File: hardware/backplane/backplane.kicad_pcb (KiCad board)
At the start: 2 copper layers, 100 x 50 mm, 50 parts, among them J1 Conn_01x04_Male, J10 Conn_02x10_Odd_Even, J13 Conn_01x08_Male, J2 RJ45_LED, J5 RJ45_LED, J6 Raspberry_Pi_2_3, J9 Conn_02x10_Odd_Even, U1 TXB0102DCU, U2 TXB0102DCU, U3 TXB0102DCU, U4 MCP23017_SO, U5 WAVGAT_CAN

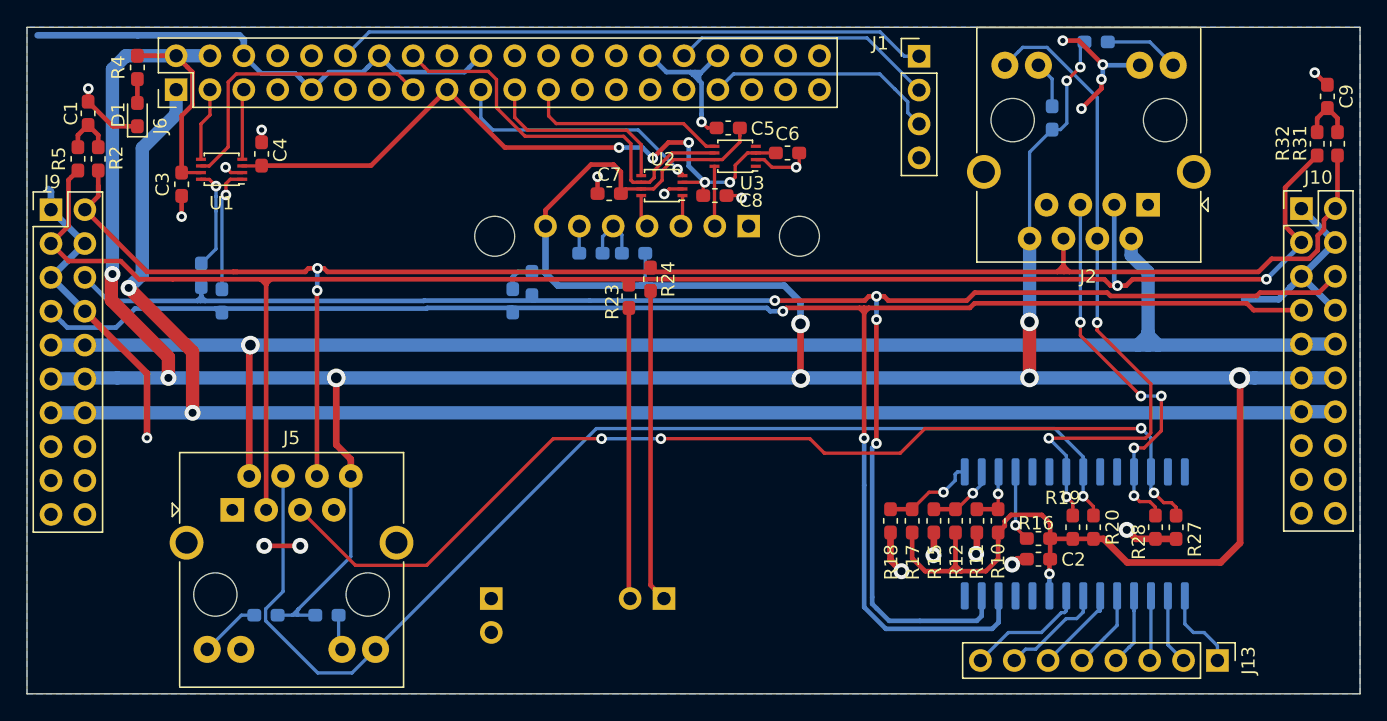
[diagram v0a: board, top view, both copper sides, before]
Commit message: Reorient RJ45 connectors in backplane, make interrupt pins accessible in IO Expanders
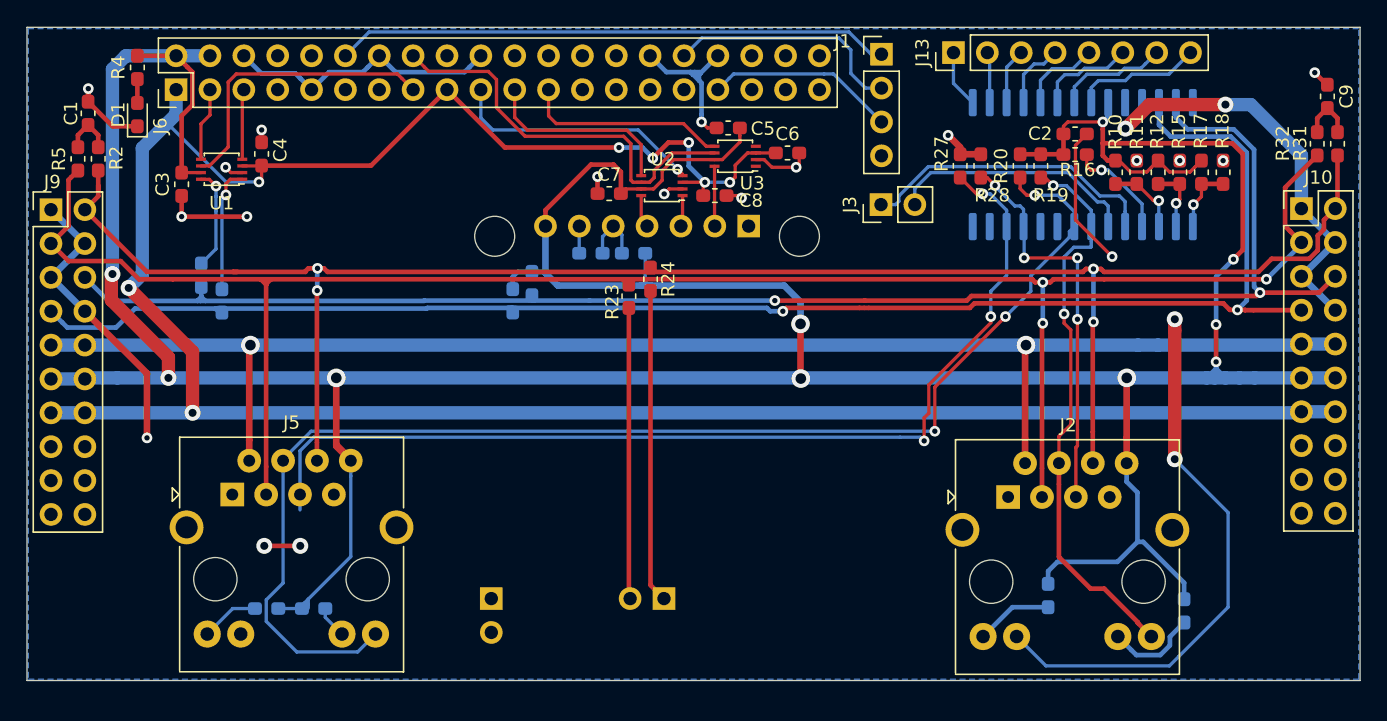
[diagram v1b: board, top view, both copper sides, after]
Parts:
- added J3: Conn_01x02_Male-Connector, Connector_PinHeader_2.54mm:PinHeader_1x02_P2.54mm_Vertical, F.Cu at (144.1, 83.3)
- moved J13 49.7 mm to (149.5, 71.9), turned to 90 degrees
- moved R3 41.7 mm to (156.6, 112.6), turned to 270 degrees
- moved R1 38.3 mm to (166.8, 113.8), turned to 270 degrees
- moved R18 36.1 mm to (169.7, 80.9), turned to 90 degrees
- moved R17 34.0 mm to (168.1, 80.9), turned to 90 degrees
- moved C2 32.0 mm to (158.6, 78.0), turned to 0 degrees
- moved R15 32.0 mm to (166.5, 80.9), turned to 90 degrees
- moved R27 31.6 mm to (150.0, 80.4), turned to 270 degrees
- moved R12 30.2 mm to (164.8, 80.9), turned to 90 degrees
- moved R28 30.1 mm to (151.6, 80.4), turned to 270 degrees
- moved R16 28.9 mm to (158.6, 79.5), turned to 180 degrees
- moved R11 28.8 mm to (163.2, 80.9), turned to 90 degrees
- moved U4 27.7 mm to (159.2, 80.3), turned to 270 degrees
- moved R20 27.7 mm to (154.5, 80.4), turned to 90 degrees
- moved R10 27.6 mm to (161.7, 80.9), turned to 90 degrees
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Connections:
- U4 pad 19: (no net) -> Net-(J3-Pad1)
- U4 pad 20: (no net) -> Net-(J3-Pad2)
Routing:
- net GND: track 137.1 -> 172.1 mm, vias 22 -> 23
- net Net-(J3-Pad1): track 0.00 -> 22.7 mm
- net Net-(J3-Pad2): track 0.00 -> 18.8 mm
- net /SCL: track 135.2 -> 118.0 mm
- net /SDA: track 131.8 -> 116.6 mm, vias 4 -> 2
- net WIRE_GOOD_1: track 87.6 -> 98.6 mm, vias 1 -> 3
- net +3V3: track 175.5 -> 185.6 mm, vias 7 -> 8
- net /CANBUS_HIGH: track 128.2 -> 138.0 mm, vias 2 -> 4
- net /CANBUS_LOW: track 135.7 -> 144.3 mm, vias 2 -> 3
- net WIRE_GOOD_0: track 50.2 -> 42.4 mm, vias 3 -> 2
- net Net-(J2-Pad10): track 3.50 -> 6.94 mm
- net Net-(J1-Pad3): track 17.6 -> 14.3 mm
- net +12V: track 117.0 -> 113.9 mm, vias 1 -> 2
- net Net-(J1-Pad1): track 44.5 -> 41.6 mm
- net Net-(R16-Pad1): track 5.35 -> 7.88 mm
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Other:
- board size 100 x 50 mm -> 100 x 49 mm

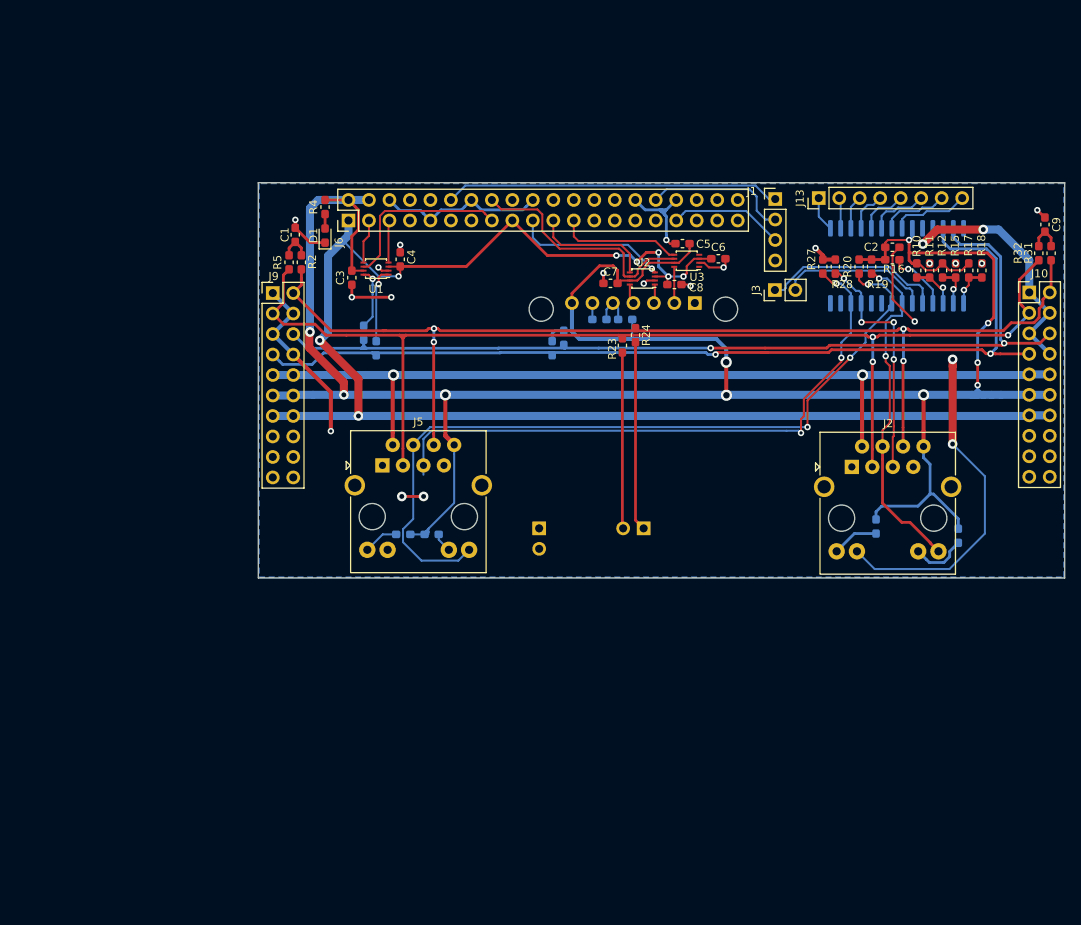
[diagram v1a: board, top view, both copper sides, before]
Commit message: New backplane schematic
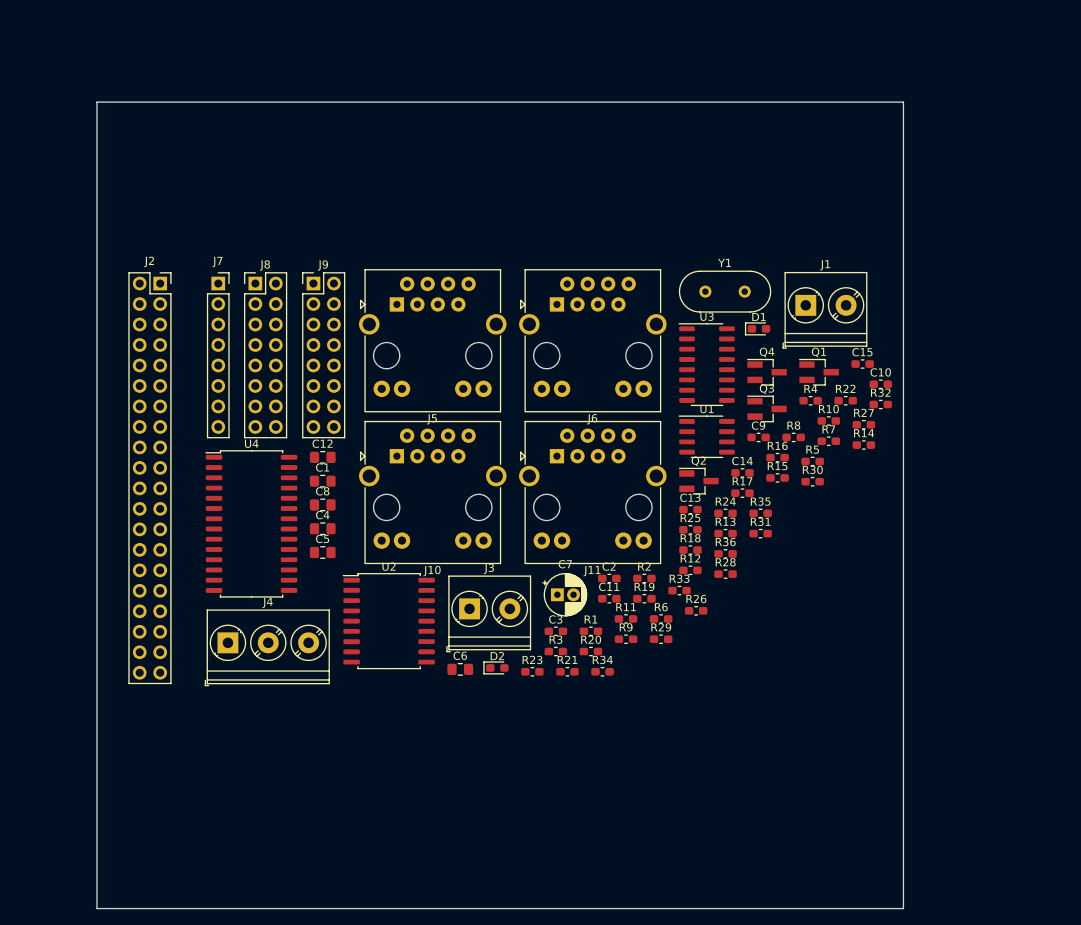
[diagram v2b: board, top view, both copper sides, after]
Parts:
- removed J13: Conn_01x08_Male, Connector_PinHeader_2.54mm:PinHeader_1x08_P2.54mm_Vertical
- removed U5: WAVGAT_CAN, WAVGAT_CAN:WAVGAT_CAN
- added C10: 100n, Capacitor_SMD:C_0603_1608Metric_Pad1.05x0.95mm_HandSolder, F.Cu at (157.2, 95.0)
- added C11: 22p, Capacitor_SMD:C_0603_1608Metric_Pad1.05x0.95mm_HandSolder, F.Cu at (123.5, 121.6)
- added C12: 470n, Capacitor_SMD:C_0805_2012Metric_Pad1.15x1.40mm_HandSolder, F.Cu at (88.0, 104.0)
- added C13: 4n7, Capacitor_SMD:C_0603_1608Metric_Pad1.05x0.95mm_HandSolder, F.Cu at (133.6, 110.5)
- added C14: 4n7, Capacitor_SMD:C_0603_1608Metric_Pad1.05x0.95mm_HandSolder, F.Cu at (140.0, 106.0)
- added C15: 100n, Capacitor_SMD:C_0603_1608Metric_Pad1.05x0.95mm_HandSolder, F.Cu at (154.9, 92.5)
- added D2: LED, LED_SMD:LED_0603_1608Metric_Pad1.05x0.95mm_HandSolder, F.Cu at (109.6, 130.2)
- added J11: RJ45_LED, Connector_RJ:RJ45_BEL_SS74301-00x_Vertical, F.Cu at (117.0, 103.9)
- added J4: Screw_Terminal_01x03, TerminalBlock_Phoenix:TerminalBlock_Phoenix_PT-1,5-3-5.0-H_1x03_P5.00mm_Horizontal, F.Cu at (76.2, 127.0)
- added J7: Conn_01x08_Female, Connector_PinSocket_2.54mm:PinSocket_1x08_P2.54mm_Vertical, F.Cu at (75.0, 82.5)
- added J8: Conn_02x08_Odd_Even, Connector_PinHeader_2.54mm:PinHeader_2x08_P2.54mm_Vertical, F.Cu at (79.6, 82.5)
- added Q1: Q_NMOS_GSD, Package_TO_SOT_SMD:SOT-23_Handsoldering, F.Cu at (149.5, 93.5)
- added Q2: Q_NMOS_GSD, Package_TO_SOT_SMD:SOT-23_Handsoldering, F.Cu at (134.6, 107.0)
- added Q3: Q_NMOS_GSD, Package_TO_SOT_SMD:SOT-23_Handsoldering, F.Cu at (143.1, 98.0)
- added Q4: Q_NMOS_GSD, Package_TO_SOT_SMD:SOT-23_Handsoldering, F.Cu at (143.1, 93.5)
- added R21: 560R, Resistor_SMD:R_0603_1608Metric_Pad1.05x0.95mm_HandSolder, F.Cu at (118.3, 130.6)
- added R22: 60R, Resistor_SMD:R_0603_1608Metric_Pad1.05x0.95mm_HandSolder, F.Cu at (152.8, 97.0)
- added R25: 560R, Resistor_SMD:R_0603_1608Metric_Pad1.05x0.95mm_HandSolder, F.Cu at (133.6, 113.0)
- added R26: 4K7, Resistor_SMD:R_0603_1608Metric_Pad1.05x0.95mm_HandSolder, F.Cu at (134.3, 123.1)
- added R33: 4K7, Resistor_SMD:R_0603_1608Metric_Pad1.05x0.95mm_HandSolder, F.Cu at (132.2, 120.6)
- added R34: 4K7, Resistor_SMD:R_0603_1608Metric_Pad1.05x0.95mm_HandSolder, F.Cu at (122.7, 130.6)
- added R35: 4K7, Resistor_SMD:R_0603_1608Metric_Pad1.05x0.95mm_HandSolder, F.Cu at (142.3, 111.0)
- added R36: 4K7, Resistor_SMD:R_0603_1608Metric_Pad1.05x0.95mm_HandSolder, F.Cu at (137.9, 116.0)
- added Y1: 8MHz, Crystal:Crystal_HC49-U_Vertical, F.Cu at (135.4, 83.5)
- C1: value 4n7 -> 10u; footprint Capacitor_SMD:C_0603_1608Metric_Pad1.05x0.95mm_HandSolder -> Capacitor_SMD:C_0805_2012Metric_Pad1.15x1.40mm_HandSolder
- C2, C3: value 0.1uF -> 100n
- C4, C5, C6: value 0.1uF -> 1u; footprint Capacitor_SMD:C_0603_1608Metric_Pad1.05x0.95mm_HandSolder -> Capacitor_SMD:C_0805_2012Metric_Pad1.15x1.40mm_HandSolder
- C7: value 0.1uF -> 47u; footprint Capacitor_SMD:C_0603_1608Metric_Pad1.05x0.95mm_HandSolder -> Capacitor_THT:CP_Radial_D5.0mm_P2.00mm
- C8: value 0.1uF -> 470n; footprint Capacitor_SMD:C_0603_1608Metric_Pad1.05x0.95mm_HandSolder -> Capacitor_SMD:C_0805_2012Metric_Pad1.15x1.40mm_HandSolder
- C9: value 4n7 -> 22p
- J1: value Conn_01x04_Male -> Screw_Terminal_01x02; footprint Connector_PinHeader_2.54mm:PinHeader_1x04_P2.54mm_Vertical -> TerminalBlock_Phoenix:TerminalBlock_Phoenix_PT-1,5-2-5.0-H_1x02_P5.00mm_Horizontal
- J10: value Conn_02x10_Odd_Even -> RJ45_LED; footprint Connector_PinHeader_2.54mm:PinHeader_2x10_P2.54mm_Vertical -> Connector_RJ:RJ45_BEL_SS74301-00x_Vertical
- J2: value RJ45_LED -> Raspberry_Pi_2_3; footprint Connector_RJ:RJ45_BEL_SS74301-00x_Vertical -> Connector_PinSocket_2.54mm:PinSocket_2x20_P2.54mm_Vertical
- J3: value Conn_01x02_Male-Connector -> Screw_Terminal_01x02; footprint Connector_PinHeader_2.54mm:PinHeader_1x02_P2.54mm_Vertical -> TerminalBlock_Phoenix:TerminalBlock_Phoenix_PT-1,5-2-5.0-H_1x02_P5.00mm_Horizontal
- J6: value Raspberry_Pi_2_3 -> RJ45_LED; footprint Connector_PinHeader_2.54mm:PinHeader_2x20_P2.54mm_Vertical -> Connector_RJ:RJ45_BEL_SS74301-00x_Vertical
- J9: value Conn_02x10_Odd_Even -> Conn_02x08_Odd_Even; footprint Connector_PinHeader_2.54mm:PinHeader_2x10_P2.54mm_Vertical -> Connector_PinHeader_2.54mm:PinHeader_2x08_P2.54mm_Vertical
- R1, R8, R9: value 560R -> 10k; moved to F.Cu
- R10: value 4K7 -> 560R
- R11: value 4K7 -> 2k
- R12, R15: value 4K7 -> 10k
- R13, R14: value 0R -> 10k; moved to F.Cu
- R16, R17: value 4K7 -> 0R
- R18: value 4K7 -> 60R
- R19: value 10K -> 60R
- R2, R5: value 60R -> 10k
- R20, R27, R28: value 10K -> 560R
- R23: value 0R -> 60R
- R24: value 0R -> 560R
- R29, R30: value 4K7 -> 560R; moved to F.Cu
- R3: value 560R -> 0R; moved to F.Cu
- R31, R32: value 60R -> 4K7
- R4: value 560R -> 0R
- R6, R7: value 4K7 -> 10k; moved to F.Cu
- U1: value TXB0102DCU -> TJA1051T; footprint Package_SO:VSSOP-8_2.4x2.1mm_P0.5mm -> Package_SO:SOIC-8_3.9x4.9mm_P1.27mm
- U2: value TXB0102DCU -> MCP2515-xSO; footprint Package_SO:VSSOP-8_2.4x2.1mm_P0.5mm -> Package_SO:SOIC-18W_7.5x11.6mm_P1.27mm
- U3: value TXB0102DCU -> PAM8403; footprint Package_SO:VSSOP-8_2.4x2.1mm_P0.5mm -> Package_SO:SOIC-16_3.9x9.9mm_P1.27mm
- U4: moved to F.Cu
- moved J2 88.7 mm to (67.8, 82.5)
- moved U4 86.2 mm to (79.2, 112.3), turned to 0 degrees
- moved J10 81.0 mm to (97.2, 103.9)
- moved R5 69.5 mm to (148.7, 104.6), turned to 0 degrees
- moved R4 64.8 mm to (148.5, 97.0), turned to 0 degrees
- moved R14 63.6 mm to (155.1, 102.5), turned to 0 degrees
- moved C6 60.1 mm to (105.0, 130.3)
- moved C5 58.8 mm to (88.0, 115.8)
- moved R20 58.2 mm to (121.2, 128.1), turned to 0 degrees
- moved R2 57.8 mm to (127.9, 119.1), turned to 0 degrees
- moved R11 57.3 mm to (125.6, 124.1), turned to 0 degrees
- moved D1 55.0 mm to (142.1, 88.1), turned to 0 degrees
- moved J3 54.7 mm to (106.2, 122.8), turned to 0 degrees
- moved C2 54.0 mm to (123.5, 119.1)
- moved U2 52.8 mm to (96.2, 124.4), turned to 0 degrees
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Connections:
- C1 pad 1: GND -> +3V3
- C1 pad 2: Net-(C1-Pad2) -> GND
- C3 pad 1: GND -> +3V3
- C3 pad 2: VCC -> GND
- C4 pad 1: +3V3 -> VCC
- C5 pad 1: GND -> VCC
- C5 pad 2: VCC -> GND
- C6 pad 1: +3V3 -> VCC
- C7 pad 1: GND -> VCC
- C7 pad 2: VCC -> GND
- C8 pad 1: +3V3 -> Net-(C8-Pad1)
- C8 pad 2: GND -> AUDIO_L
- C9 pad 1: GND -> Net-(C9-Pad1)
- C9 pad 2: Net-(C9-Pad2) -> GND
- J1 pad 1: Net-(J1-Pad1) -> /SPKR_L+
- J1 pad 2: Net-(J1-Pad2) -> /SPKR_L-
- J10 pad 10: +12V -> Net-(J10-Pad10)
- J10 pad 11: VCC -> MODULE_READY_2
- J10 pad 12: VCC -> Net-(J10-Pad12)
- J10 pad 2: /CANBUS_HIGH -> +12V
- J10 pad 3: /CANBUS_LOW -> CAN_L
- J10 pad 4: GND -> MODULE_READY_2
- J10 pad 5: GND -> MODULE_ENABLE_2
- J10 pad 6: /SDA -> CAN_H
- J10 pad 7: /SCL -> GND
- J10 pad 8: GND -> VCC
- J10 pad 9: +12V -> MODULE_ENABLE_2
- J2 pad 1: GND -> +3V3
- J2 pad 11: GND -> Net-(J2-Pad11)
- J2 pad 2: +12V -> VCC
- J2 pad 3: /CANBUS_LOW -> SDA_3V3
- J2 pad 4: WIRE_GOOD_0 -> VCC
- J2 pad 5: MODULE_GOOD_0 -> SCL_3V3
- J2 pad 6: /CANBUS_HIGH -> GND
- J2 pad 7: GND -> Net-(J2-Pad7)
- J2 pad 8: VCC -> Net-(J2-Pad8)
- J2 pad 9: WIRE_GOOD_0 -> GND
- J3 pad 1: Net-(J3-Pad1) -> /SPKR_R-
- J3 pad 2: Net-(J3-Pad2) -> /SPKR_R+
- J5 pad 11: GND -> MODULE_READY_0
- J5 pad 3: /CANBUS_LOW -> CAN_L
- J5 pad 4: WIRE_GOOD_1 -> MODULE_READY_0
- J5 pad 5: MODULE_GOOD_1 -> MODULE_ENABLE_0
- J5 pad 6: /CANBUS_HIGH -> CAN_H
- J5 pad 9: WIRE_GOOD_1 -> MODULE_ENABLE_0
- J5 pad SH: (no net) -> GND
- J6 pad 1: +3V3 -> GND
- J6 pad 10: (no net) -> Net-(J6-Pad10)
- J6 pad 11: (no net) -> MODULE_READY_1
- J6 pad 12: Net-(J1-Pad1) -> Net-(J6-Pad12)
- J6 pad 2: VCC -> +12V
- J6 pad 3: Net-(J6-Pad3) -> CAN_L
- J6 pad 4: VCC -> MODULE_READY_1
- J6 pad 5: Net-(J6-Pad5) -> MODULE_ENABLE_1
- J6 pad 6: GND -> CAN_H
- J6 pad 7: (no net) -> GND
- J6 pad 8: (no net) -> VCC
- J6 pad 9: GND -> MODULE_ENABLE_1
- J9 pad 15: (no net) -> Net-(J9-Pad15)
- J9 pad 16: (no net) -> Net-(J9-Pad16)
- J9 pad 2: /CANBUS_HIGH -> CAN_H
- J9 pad 3: /CANBUS_LOW -> CAN_L
- J9 pad 6: /SDA -> SDA
- J9 pad 7: /SCL -> SCL
- R1 pad 1: VCC -> +3V3
- R1 pad 2: Net-(J2-Pad10) -> Net-(Q1-Pad2)
- R10 pad 1: Net-(R10-Pad1) -> VCC
- R10 pad 2: VCC -> Net-(D1-Pad2)
- R11 pad 1: Net-(R10-Pad1) -> +12V
- R11 pad 2: GND -> Net-(D2-Pad2)
- R12 pad 1: Net-(R12-Pad1) -> +3V3
- R12 pad 2: VCC -> SCL_3V3
- R13 pad 1: /SCL -> VCC
- R13 pad 2: Net-(R13-Pad2) -> Net-(Q3-Pad3)
- R14 pad 1: Net-(R14-Pad1) -> +3V3
- R14 pad 2: /SDA -> SDA_3V3
- R15 pad 1: Net-(R12-Pad1) -> VCC
- R15 pad 2: GND -> Net-(Q4-Pad3)
- R16 pad 1: Net-(R16-Pad1) -> SCL
- R16 pad 2: VCC -> Net-(Q3-Pad3)
- R17 pad 1: Net-(R17-Pad1) -> SDA
- R17 pad 2: VCC -> Net-(Q4-Pad3)
- R18 pad 1: Net-(R17-Pad1) -> CAN_H
- R18 pad 2: GND -> Net-(C13-Pad1)
- R19 pad 1: WIRE_GOOD_0 -> CAN_H
- R19 pad 2: VCC -> Net-(C14-Pad1)
- R2 pad 1: /CANBUS_HIGH -> VCC
- R2 pad 2: Net-(C1-Pad2) -> Net-(Q1-Pad3)
- R20 pad 1: WIRE_GOOD_1 -> VCC
- R20 pad 2: VCC -> Net-(J5-Pad10)
- R23 pad 1: /CANBUS_LOW -> CAN_L
- R23 pad 2: Net-(R23-Pad2) -> Net-(C14-Pad1)
- R24 pad 1: Net-(R24-Pad1) -> VCC
- R24 pad 2: /CANBUS_HIGH -> Net-(J5-Pad12)
- R27 pad 1: GND -> VCC
- R27 pad 2: MODULE_GOOD_1 -> Net-(J10-Pad10)
- R28 pad 1: GND -> VCC
- R28 pad 2: MODULE_GOOD_0 -> Net-(J11-Pad10)
- R29 pad 1: Net-(R29-Pad1) -> VCC
- R29 pad 2: GND -> Net-(J10-Pad12)
- R3 pad 1: VCC -> CAN_H
- R3 pad 2: Net-(J2-Pad12) -> Net-(R3-Pad2)
- R30 pad 1: Net-(R29-Pad1) -> VCC
- R30 pad 2: VCC -> Net-(J11-Pad12)
- R31 pad 1: /CANBUS_HIGH -> Net-(R31-Pad1)
- R31 pad 2: Net-(C9-Pad2) -> VCC
- R32 pad 1: /CANBUS_LOW -> Net-(R31-Pad1)
- R32 pad 2: Net-(C9-Pad2) -> GND
- R4 pad 1: Net-(D1-Pad2) -> CAN_L
- R4 pad 2: VCC -> Net-(R4-Pad2)
- R5 pad 1: /CANBUS_LOW -> Net-(R5-Pad1)
- R5 pad 2: Net-(C1-Pad2) -> Net-(C8-Pad1)
- R6 pad 1: /SDA -> +3V3
- R6 pad 2: VCC -> Net-(Q2-Pad2)
- R7 pad 1: /SCL -> VCC
- R7 pad 2: VCC -> Net-(Q2-Pad3)
- R8 pad 1: VCC -> Net-(R8-Pad1)
- R8 pad 2: Net-(J5-Pad10) -> Net-(C12-Pad1)
- R9 pad 1: VCC -> +3V3
- R9 pad 2: Net-(J5-Pad12) -> Net-(R9-Pad2)
- U1 pad 1: Net-(R13-Pad2) -> Net-(Q2-Pad3)
- U1 pad 3: +3V3 -> VCC
- U1 pad 4: Net-(J6-Pad5) -> Net-(Q1-Pad3)
- U1 pad 5: Net-(J6-Pad3) -> Net-(U1-Pad5)
- U1 pad 6: Net-(J6-Pad15) -> Net-(R4-Pad2)
- U1 pad 7: VCC -> Net-(R3-Pad2)
- U1 pad 8: Net-(R14-Pad1) -> Net-(U1-Pad8)
- U2 pad 1: Net-(U2-Pad1) -> Net-(Q2-Pad2)
- U2 pad 2: GND -> Net-(Q1-Pad2)
- U2 pad 3: +3V3 -> Net-(U2-Pad3)
- U2 pad 4: Net-(J6-Pad19) -> Net-(U2-Pad4)
- U2 pad 5: Net-(J6-Pad21) -> Net-(U2-Pad5)
- U2 pad 6: Net-(J6-Pad16) -> Net-(U2-Pad6)
- U2 pad 7: VCC -> Net-(C9-Pad1)
- U3 pad 1: (no net) -> /SPKR_L+
- U3 pad 3: +3V3 -> /SPKR_L-
- U3 pad 4: (no net) -> VCC
- U3 pad 5: Net-(J6-Pad23) -> Net-(U3-Pad5)
- U3 pad 6: Net-(J6-Pad16) -> VCC
- U3 pad 7: VCC -> Net-(R5-Pad1)
- U4 pad 11: (no net) -> Net-(U4-Pad11)
- U4 pad 12: /SCL -> SCL
- U4 pad 13: /SDA -> SDA
- U4 pad 14: (no net) -> Net-(U4-Pad14)
- U4 pad 15: Net-(R17-Pad1) -> Net-(R35-Pad1)
- U4 pad 16: Net-(R12-Pad1) -> Net-(R33-Pad1)
- U4 pad 17: Net-(R10-Pad1) -> Net-(R31-Pad1)
- U4 pad 18: Net-(R16-Pad1) -> Net-(R26-Pad1)
- U4 pad 19: Net-(J3-Pad1) -> Net-(U4-Pad19)
- U4 pad 20: Net-(J3-Pad2) -> MCP23017_INT
- U4 pad 21: WIRE_GOOD_0 -> MODULE_ENABLE_0
- U4 pad 22: WIRE_GOOD_1 -> MODULE_ENABLE_1
- U4 pad 23: (no net) -> MODULE_ENABLE_2
- U4 pad 24: (no net) -> MODULE_ENABLE_3
- U4 pad 25: MODULE_GOOD_0 -> MODULE_READY_0
- U4 pad 26: MODULE_GOOD_1 -> MODULE_READY_1
- U4 pad 27: (no net) -> MODULE_READY_2
- U4 pad 28: (no net) -> MODULE_READY_3
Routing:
- net VCC: track 304.6 -> 0.00 mm, vias 10 -> 0
- net +3V3: track 185.6 -> 0.00 mm, vias 8 -> 0
- net GND: track 172.1 -> 0.00 mm, vias 23 -> 0
- net /CANBUS_LOW: track 144.3 -> 0.00 mm, vias 3 -> 0
- net /CANBUS_HIGH: track 138.0 -> 0.00 mm, vias 4 -> 0
- net /SCL: track 118.0 -> 0.00 mm, vias 2 -> 0
- net /SDA: track 116.6 -> 0.00 mm, vias 2 -> 0
- net +12V: track 113.9 -> 0.00 mm, vias 2 -> 0
- net WIRE_GOOD_1: track 98.6 -> 0.00 mm, vias 3 -> 0
- net MODULE_GOOD_1: track 76.2 -> 0.00 mm, vias 3 -> 0
- net WIRE_GOOD_0: track 42.4 -> 0.00 mm, vias 2 -> 0
- net Net-(J1-Pad1): track 41.6 -> 0.00 mm
- net Net-(J6-Pad16): track 30.6 -> 0.00 mm
- net MODULE_GOOD_0: track 29.9 -> 0.00 mm, vias 4 -> 0
- net Net-(R24-Pad1): track 23.5 -> 0.00 mm
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- removed copper zone on B.Cu, net GND
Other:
- board size 100 x 49 mm -> 100 x 100 mm
